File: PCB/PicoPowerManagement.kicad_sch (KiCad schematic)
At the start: 25 parts, among them J1 Conn_02x07_Odd_Even, J10 Conn_02x07_Odd_Even, J11 NAS Fan 1, J12 NAS Fan 2, J13 ATX 24P Connection, J15 Conn_01x02, J2 Conn_02x07_Odd_Even, J3 UART Header, J4 DEBUG, J5 SwitchLEDS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

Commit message: confused now
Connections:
- net +12V: now also J10.1 (Pin_1), J10.3 (Pin_3), J7.1 (Pin_1), J7.3 (Pin_3), J9.1 (Pin_1), J9.3 (Pin_3); no longer J10.11 (Pin_11), J10.13 (Pin_13), J7.11 (Pin_11), J7.13 (Pin_13), J9.11 (Pin_11), J9.13 (Pin_13)
- net +3.3V: now also J10.14 (Pin_14), J7.14 (Pin_14), J9.14 (Pin_14)
- net +5V: now also J10.2 (Pin_2), J10.4 (Pin_4), J7.2 (Pin_2), J7.4 (Pin_4), J9.2 (Pin_2), J9.4 (Pin_4); no longer J10.12 (Pin_12), J10.14 (Pin_14), J7.12 (Pin_12), J7.14 (Pin_14), J9.12 (Pin_12), J9.14 (Pin_14)
- net GND: now also J10.5 (Pin_5), J10.6 (Pin_6), J7.5 (Pin_5), J7.6 (Pin_6), J9.5 (Pin_5), J9.6 (Pin_6); no longer J10.10 (Pin_10), J10.7 (Pin_7), J10.9 (Pin_9), J7.10 (Pin_10), J7.7 (Pin_7), J7.9 (Pin_9), J9.10 (Pin_10), J9.7 (Pin_7), J9.9 (Pin_9)
- net SCL0: now also J9.12 (Pin_12); no longer J9.8 (Pin_8)
- net SCL1: now also J10.12 (Pin_12), J7.12 (Pin_12); no longer J10.8 (Pin_8), J7.8 (Pin_8)
- net SDA0: now also J9.10 (Pin_10); no longer J9.6 (Pin_6)
- net SDA1: now also J10.10 (Pin_10), J7.10 (Pin_10); no longer J10.6 (Pin_6), J7.6 (Pin_6)
- net USB2_12VEN: now also J9.8 (Pin_8); no longer J9.1 (Pin_1)
- net USB2_5VEN: now also J9.7 (Pin_7); no longer J9.3 (Pin_3)
- net USB2_INT: now also J9.9 (Pin_9); no longer J9.5 (Pin_5)
- net USB4_12VEN: now also J7.8 (Pin_8); no longer J7.1 (Pin_1)
- net USB4_5VEN: now also J7.7 (Pin_7); no longer J7.3 (Pin_3)
- net USB4_INT: now also J7.9 (Pin_9); no longer J7.5 (Pin_5)
- net USB5_12VEN: now also J10.8 (Pin_8); no longer J10.1 (Pin_1)
- net USB5_5VEN: now also J10.7 (Pin_7); no longer J10.3 (Pin_3)
- net USB5_INT: now also J10.9 (Pin_9); no longer J10.5 (Pin_5)
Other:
- moved on the sheet: J10, J11, J12, J7, J9

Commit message: Enhance PCB design and update UI for Raspberry Pi models
The most important changes in the `PicoPowerManagement.kicad_pcb` file focus on improving the PCB design's functionality and visual representation. Key updates include the removal of the option to plot invisible text and the addition of multiple mounting hole footprints with specific properties. Significant modifications were made to the layout, including adjustments to segments and paths to ensure compliance with updated specifications.

In the `PicoPowerManagement.kicad_pro` file, a new error check for "text_on_edge_cuts" was added to enhance the validation process. The `PicoPowerManagement.kicad_sch` files saw the addition of multiple mounting hole symbols with updated reference designators and footprints. Additionally, the `Home.razor` file was modified to display updated status information for Raspberry Pi models, changing labels from "Pi 3" and "Pi 4" to "PiDC" and "PiBuild," and adding shutdown buttons for each status display.
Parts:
- added H1, H2, H3: MountingHole, MountingHole:MountingHole_3mm, symbol Mechanical:MountingHole
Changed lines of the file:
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@@
 	)
 	(symbol
+		(lib_id "Mechanical:MountingHole")
+		(at 156.21 88.9 0)
+		(unit 1)
+		(exclude_from_sim no)
+		(in_bom no)
+		(on_board yes)
+		(dnp no)
+		(fields_autoplaced yes)
+		(property "Reference" "H3"
+			(at 158.75 87.6299 0)
+			(effects
+				(font
+					(size 1.27 1.27)
+				)
+				(justify left)
+			)
+		)
+		(property "Value" "MountingHole"
+			(at 158.75 90.1699 0)
+			(effects
+				(font
+					(size 1.27 1.27)
+				)
+				(justify left)
+			)
+		)
+		(property "Footprint" "MountingHole:MountingHole_3mm"
+			(at 156.21 88.9 0)
+			(effects
+				(font
+					(size 1.27 1.27)
+				)
+				(hide yes)
+			)
+		)
+		(property "Datasheet" "~"
+			(at 156.21 88.9 0)
+			(effects
+				(font
+					(size 1.27 1.27)
+				)
+				(hide yes)
+			)
+		)
+		(property "Description" "Mounting Hole without connection"
+			(at 156.21 88.9 0)
+			(effects
+				(font
+					(size 1.27 1.27)
+				)
+				(hide yes)
+			)
+		)
+		(instances
+			(project ""
+				(path "/450b940c-8305-4571-abac-103e5c28560c"
+					(reference "H3")
+					(unit 1)
+				)
+			)
+		)
+	)
+	(symbol
 		(lib_id "power:GND")
 		(at 13.97 45.72 0)
@@
 	)
 	(symbol
+		(lib_id "Mechanical:MountingHole")
+		(at 175.26 80.01 0)
+		(unit 1)
+		(exclude_from_sim no)
+		(in_bom no)
+		(on_board yes)
+		(dnp no)
+		(fields_autoplaced yes)
+		(property "Reference" "H2"
+			(at 177.8 78.7399 0)
+			(effects
+				(font
+					(size 1.27 1.27)
+				)
+				(justify left)
+			)
+		)
+		(property "Value" "MountingHole"
+			(at 177.8 81.2799 0)
+			(effects
+				(font
+					(size 1.27 1.27)
+				)
+				(justify left)
+			)
+		)
+		(property "Footprint" "MountingHole:MountingHole_3mm"
+			(at 175.26 80.01 0)
+			(effects
+				(font
+					(size 1.27 1.27)
+				)
+				(hide yes)
+			)
+		)
+		(property "Datasheet" "~"
+			(at 175.26 80.01 0)
+			(effects
+				(font
+					(size 1.27 1.27)
+				)
+				(hide yes)
+			)
+		)
+		(property "Description" "Mounting Hole without connection"
+			(at 175.26 80.01 0)
+			(effects
+				(font
+					(size 1.27 1.27)
+				)
+				(hide yes)
+			)
+		)
+		(instances
+			(project ""
+				(path "/450b940c-8305-4571-abac-103e5c28560c"
+					(reference "H2")
+					(unit 1)
+				)
+			)
+		)
+	)
+	(symbol
 		(lib_id "power:GND")
 		(at 104.14 99.06 0)
@@
 		(on_board yes)
 		(dnp no)
-		(property "Reference" "#PWR064"
+		(property "Reference" "#PWR0101"
 			(at 92.71 66.04 0)
 			(effects
@@
 			(project "PicoPowerManagement"
 				(path "/450b940c-8305-4571-abac-103e5c28560c"
-					(reference "#PWR064")
+					(reference "#PWR0101")
 					(unit 1)
 				)
@@
 					(unit 1)
 				)
+			)
+		)
+	)
+	(symbol
+		(lib_id "Mechanical:MountingHole")
+		(at 156.21 80.01 0)
+		(unit 1)
+		(exclude_from_sim no)
+		(in_bom no)
+		(on_board yes)
+		(dnp no)
+		(fields_autoplaced yes)
+		(property "Reference" "H1"
+			(at 158.75 78.7399 0)
+			(effects
+				(font
+					(size 1.27 1.27)
+				)
+				(justify left)
+			)
+		)
+		(property "Value" "MountingHole"
+			(at 158.75 81.2799 0)
+			(effects
+				(font
+					(size 1.27 1.27)
+				)
+				(justify left)
+			)
+		)
+		(property "Footprint" "MountingHole:MountingHole_3mm"
+			(at 156.21 80.01 0)
+			(effects
+				(font
+					(size 1.27 1.27)
+				)
+				(hide yes)
+			)
+		)
+		(property "Datasheet" "~"
+			(at 156.21 80.01 0)
+			(effects
+				(font
+					(size 1.27 1.27)
+				)
+				(hide yes)
+			)
+		)
+		(property "Description" "Mounting Hole without connection"
+			(at 156.21 80.01 0)
+			(effects
+				(font
+					(size 1.27 1.27)
+				)
+				(hide yes)
+			)
+		)
+		(instances
+			(project ""
+				(path "/450b940c-8305-4571-abac-103e5c28560c"
+					(reference "H1")
+					(unit 1)
+				)

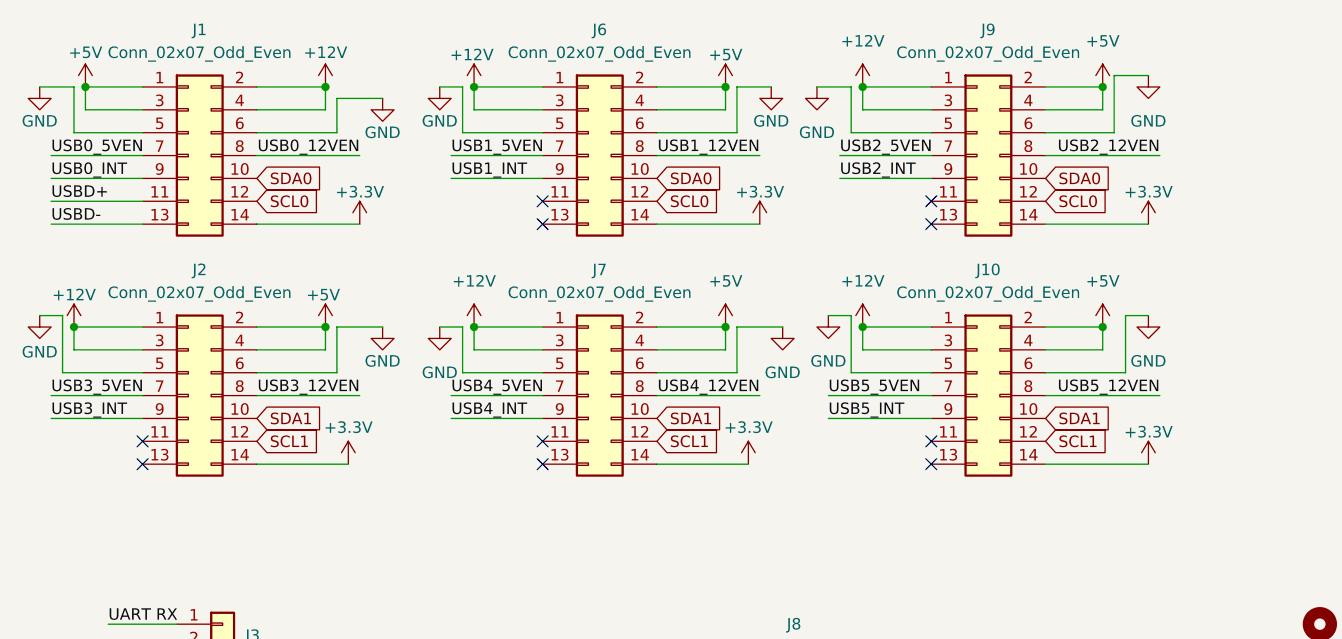
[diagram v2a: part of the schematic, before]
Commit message: simplifying USB
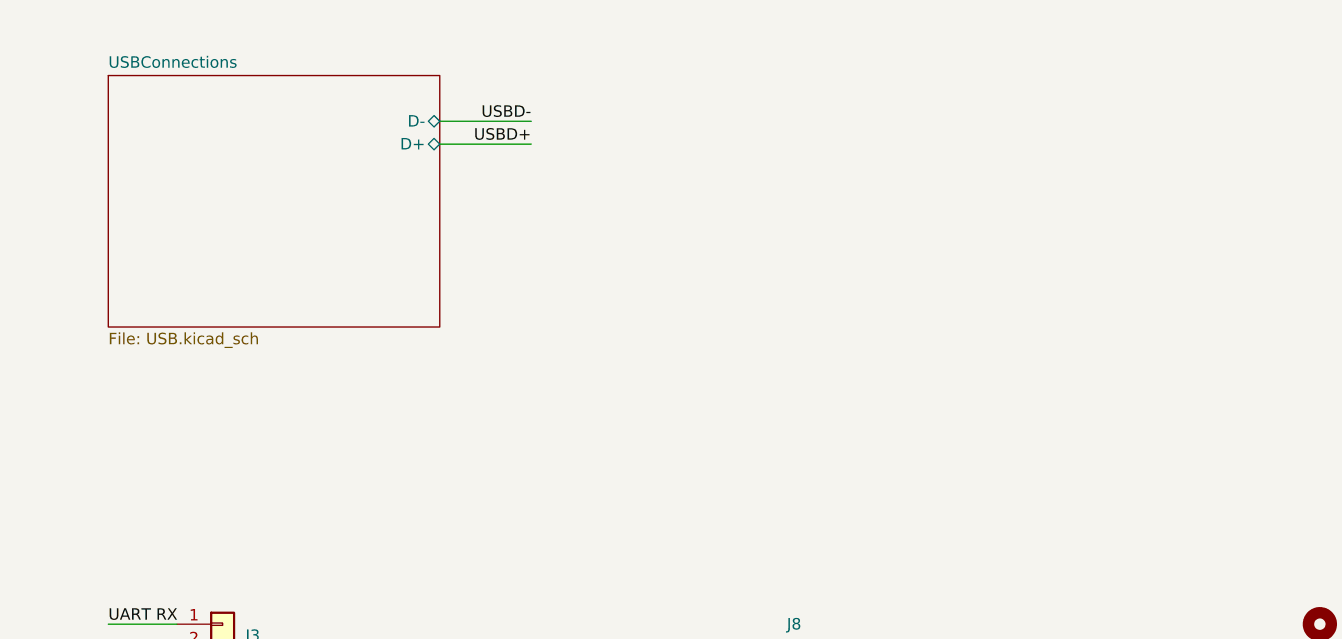
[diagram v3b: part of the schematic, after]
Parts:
- removed J1, J10, J2, J6, J7, J9: Conn_02x07_Odd_Even, Connector_PinHeader_2.54mm:PinHeader_2x07_P2.54mm_Vertical, symbol Connector_Generic:Conn_02x07_Odd_Even
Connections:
- no-connect marks 34 -> 24
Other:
- added sheet USBConnections (USB.kicad_sch)
